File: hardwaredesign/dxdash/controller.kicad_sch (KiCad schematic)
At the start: 67 parts, among them J16 uC_NRST, J17 3V3_uC, J18 SWO, J3 CAN, J4 DEBUG, J5 UART, U2 SN65HVD234, U3 STM32F103RETx, Y1 8MHz

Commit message: controller board added features
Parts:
- removed J3: CAN, Connector_PinHeader_2.54mm:PinHeader_1x03_P2.54mm_Vertical, symbol Connector:Conn_01x03_Pin
- removed R3: 1k, Resistor_SMD:R_1206_3216Metric_Pad1.30x1.75mm_HandSolder, symbol Device:R_Small
- removed R3 (x4): 220, Resistor_SMD:R_1206_3216Metric_Pad1.30x1.75mm_HandSolder, symbol Device:R_Small
- removed TP5V1 (x5): ~, TestPoint:TestPoint_THTPad_D1.0mm_Drill0.5mm, symbol Connector:TestPoint
- removed U2: SN65HVD234, Package_SO:SOIC-8_3.9x4.9mm_P1.27mm, symbol Interface_CAN_LIN:SN65HVD234
- added H1, H2, H3, H4, H5, H6, H7, H8: MountingHole, MountingHole:MountingHole_3.5mm, symbol Mechanical:MountingHole
- added J1: Conn_01x08_Pin, Connector_PinHeader_2.54mm:PinHeader_1x08_P2.54mm_Vertical, symbol Connector:Conn_01x08_Pin
- added TP2, TP3: ~, TestPoint:TestPoint_THTPad_D1.0mm_Drill0.5mm, symbol Connector:TestPoint
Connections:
- net 3V3_uC: now also J1.2 (Pin_2)
- net GND: now also J1.1 (Pin_1)
- net SPI1_CLK: now also J1.3 (Pin_3)
- net SPI1_MOSI: now also J1.4 (Pin_4)
- net uC_pwr_button: now reaches U3.43 (PA10)
- net KEEP_ON: now reaches U3.34 (PB13)
- net DISPLAY_DC: now reaches U3.26 (PB0)
- net DISPLAY_DC: now also J1.6 (Pin_6)
- net DISPLAY_RES: now reaches U3.27 (PB1)
- net DISPLAY_RES: now also J1.5 (Pin_5)
- net BUSWAKE: now reaches U3.33 (PB12)
- net ADC123_IN10 renamed uC_pot1
- net ADC123_IN11 renamed uC_pot2
- net ADC123_IN12: no longer names the net of U3.10 (PC2)
- net ADC123_IN12: now also TP2.1
- net ADC_U_HVDC: no longer names the net of U3.11 (PC3)
- net ADC_U_HVDC: now also TP3.1
- new net 5V: J1.7 (Pin_7)
- no-connect marks 0 -> 1
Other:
- note added: "display connector for ILI9341 and mounting holes"
- note removed: "CAN Transceiver"
- note removed: "CAN termination resistor. 1k does not hurt if the bus is elsewhere terminated, and helps for setup on desk without additional termination."
- note removed: "EN=High enables the transceiver. Low or open would disable it."
- note removed: "Protection resistors for the case, that the controller and the SPI slave are powered from different sources which do not synchronously turn on and off"
- note removed: "todo: EN level selectable via solder jumper"
- note removed: "todo: termination via solder jumper"

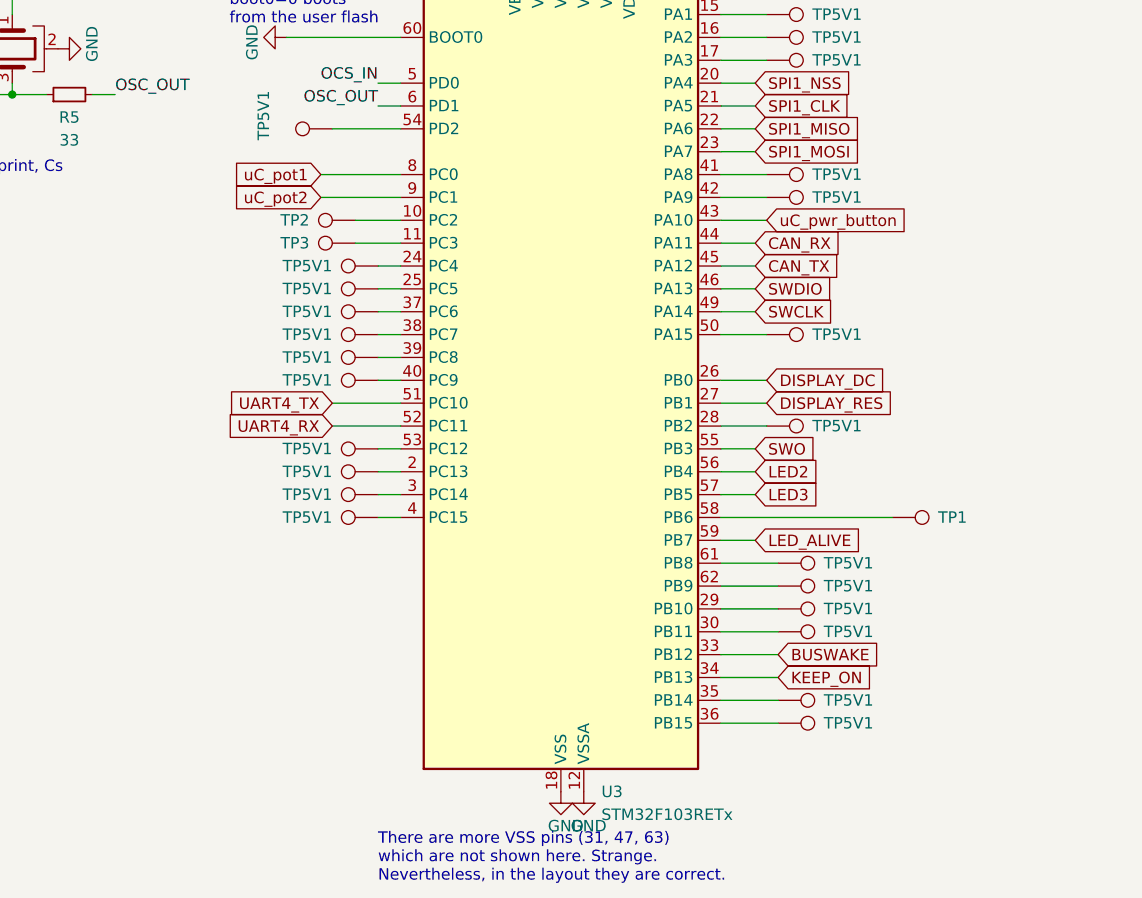
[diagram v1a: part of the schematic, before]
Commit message: added joystick
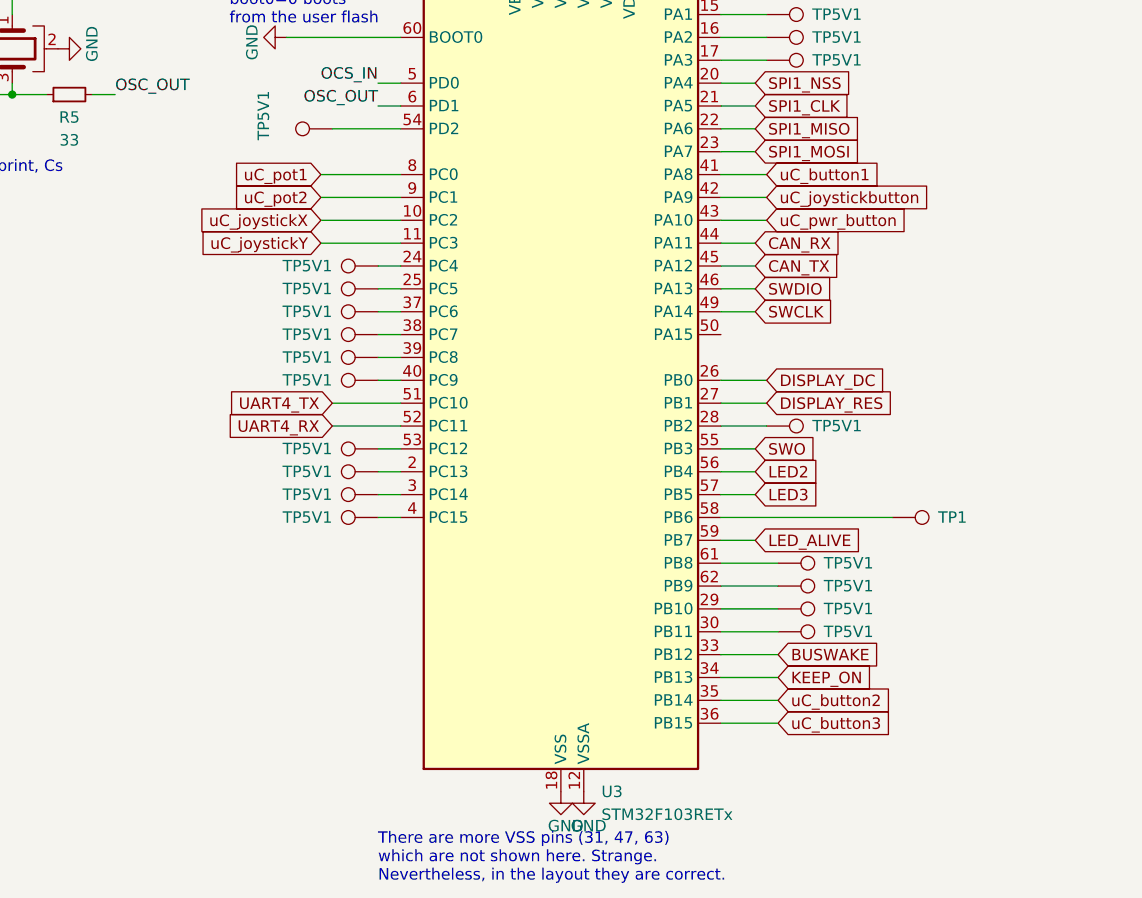
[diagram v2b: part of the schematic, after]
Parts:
- removed TP2, TP3, TP5V1 (x5): ~, TestPoint:TestPoint_THTPad_D1.0mm_Drill0.5mm, symbol Connector:TestPoint
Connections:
- net uC_button3: now reaches U3.36 (PB15)
- net uC_button1: now reaches U3.41 (PA8)
- net uC_joystickX: now reaches U3.10 (PC2)
- net uC_joystickY: now reaches U3.11 (PC3)
- net uC_joystickbutton: now reaches U3.42 (PA9)
- net uC_button2: now reaches U3.35 (PB14)

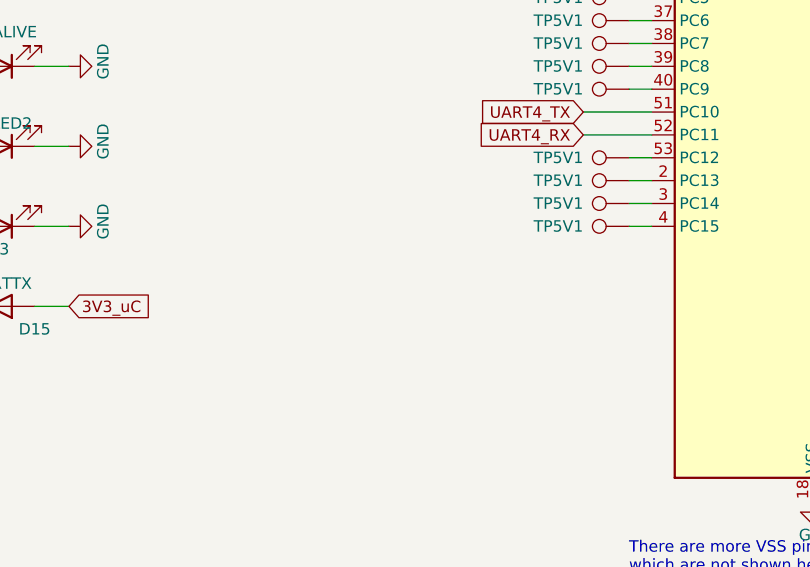
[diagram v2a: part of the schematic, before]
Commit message: added polyfuses
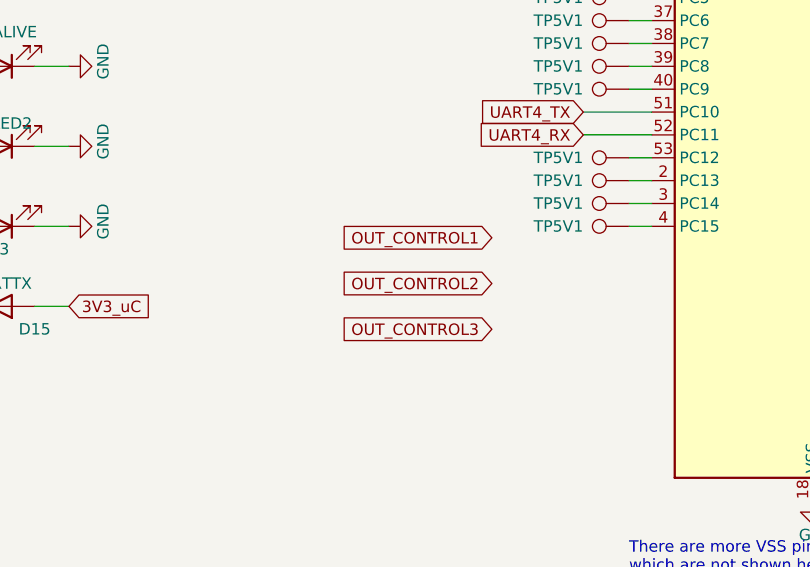
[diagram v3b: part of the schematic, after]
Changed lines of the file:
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@@
+		)
+	)
+	(global_label "OUT_CONTROL3"
+		(shape input)
+		(at 118.11 134.62 180)
+		(fields_autoplaced yes)
+		(effects
+			(font
+				(size 1.27 1.27)
+			)
+			(justify right)
+		)
+		(property "Intersheetrefs" "${INTERSHEET_REFS}"
+			(at 100.7919 134.62 0)
+			(effects
+				(font
+					(size 1.27 1.27)
+				)
+				(justify right)
+				(hide yes)
+			)
 		)
 	)
@@
 		)
 	)
+	(global_label "OUT_CONTROL1"
+		(shape input)
+		(at 118.11 124.46 180)
+		(fields_autoplaced yes)
+		(effects
+			(font
+				(size 1.27 1.27)
+			)
+			(justify right)
+		)
+		(property "Intersheetrefs" "${INTERSHEET_REFS}"
+			(at 100.7919 124.46 0)
+			(effects
+				(font
+					(size 1.27 1.27)
+				)
+				(justify right)
+				(hide yes)
+			)
+		)
+	)
 	(global_label "uC_pot2"
 		(shape input)
@@
 			(effects
 				(font
+					(size 1.27 1.27)
+				)
+				(justify right)
+				(hide yes)
+			)
+		)
+	)
+	(global_label "OUT_CONTROL2"
+		(shape input)
+		(at 118.11 129.54 180)
+		(fields_autoplaced yes)
+		(effects
+			(font
+				(size 1.27 1.27)
+			)
+			(justify right)
+		)
+		(property "Intersheetrefs" "${INTERSHEET_REFS}"
+			(at 100.7919 129.54 0)
+			(effects
+				(font

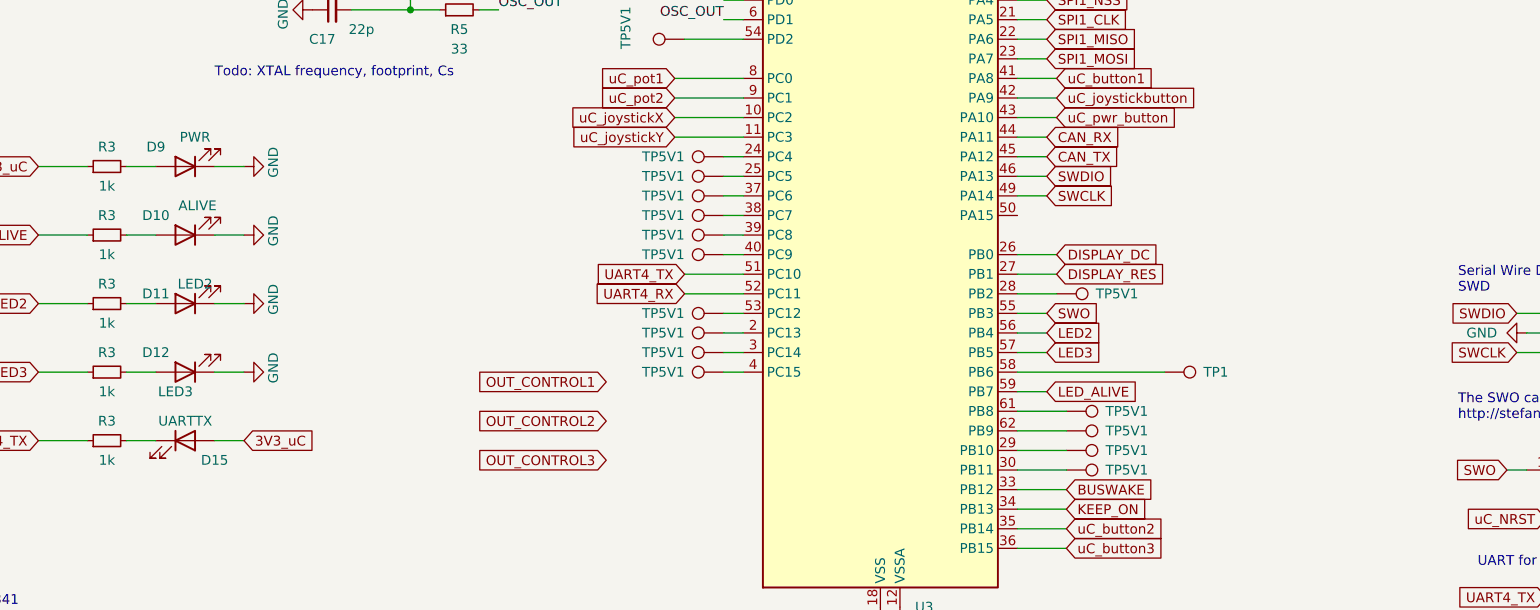
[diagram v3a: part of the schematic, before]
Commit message: added switch inputs. Layout preparation.
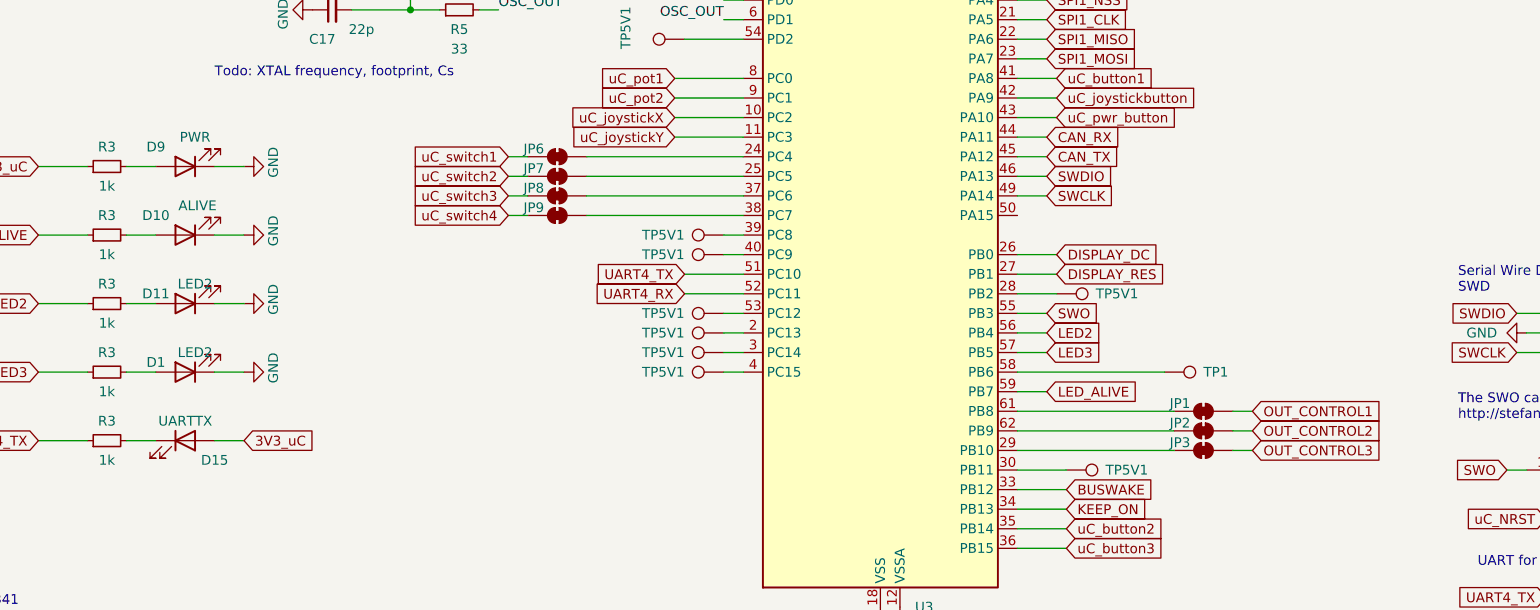
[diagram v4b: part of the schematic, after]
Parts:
- removed D12: LED3, LED_SMD:LED_0805_2012Metric_Pad1.15x1.40mm_HandSolder, symbol Device:LED
- removed TP5V1 (x7): ~, TestPoint:TestPoint_THTPad_D1.0mm_Drill0.5mm, symbol Connector:TestPoint
- added D1: LED2, LED_THT:LED_D5.0mm, symbol Device:LED
- added JP1, JP2, JP3, JP6, JP7, JP8, JP9: SolderJumper_2_Bridged, Jumper:SolderJumper-2_P1.3mm_Bridged_RoundedPad1.0x1.5mm, symbol Jumper:SolderJumper_2_Bridged
- D11: footprint LED_SMD:LED_0805_2012Metric_Pad1.15x1.40mm_HandSolder -> LED_THT:LED_D5.0mm
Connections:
- net GND: now also D1.1 (K)
- net OUT_CONTROL1: now also JP1.2 (B)
- net OUT_CONTROL2: now also JP2.2 (B)
- net OUT_CONTROL3: now also JP3.2 (B)
- net at U3.29 (PB10): now also JP3.1 (A)
- net at U3.38 (PC7): now also JP9.2 (B)
- net at U3.37 (PC6): now also JP8.2 (B)
- net at U3.24 (PC4): now also JP6.2 (B)
- net at U3.25 (PC5): now also JP7.2 (B)
- net at U3.61 (PB8): now also JP1.1 (A)
- net at U3.62 (PB9): now also JP2.1 (A)
- net at R3.2: now also D1.2 (A)
- new net uC_switch1: JP6.1 (A)
- new net uC_switch2: JP7.1 (A)
- new net uC_switch3: JP8.1 (A)
- new net uC_switch4: JP9.1 (A)

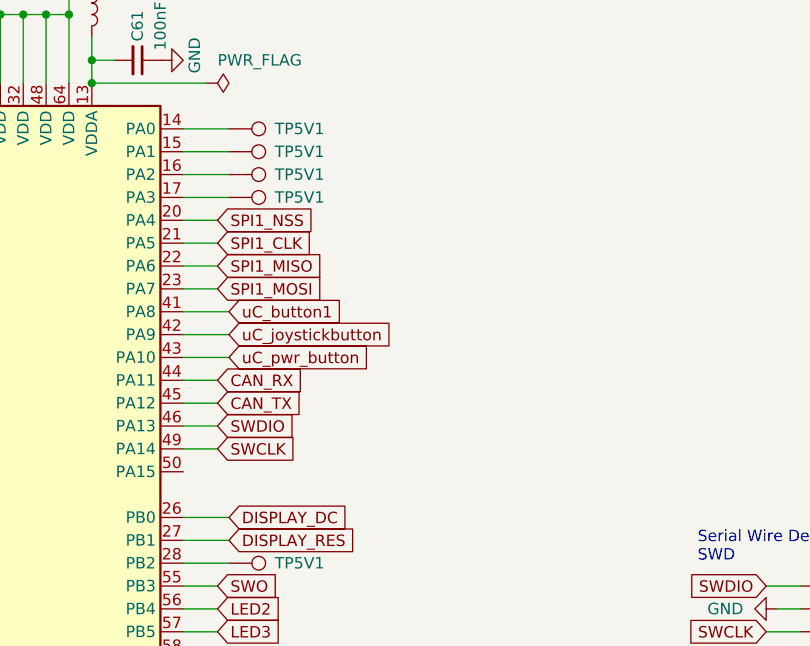
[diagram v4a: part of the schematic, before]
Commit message: board: layout finished
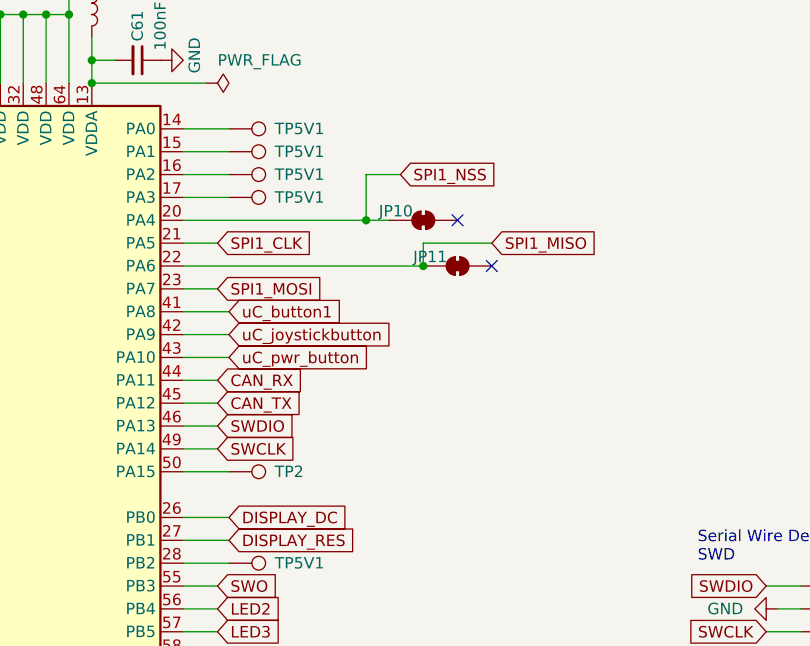
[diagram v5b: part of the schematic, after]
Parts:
- added JP10, JP11: SolderJumper_2_Bridged, Jumper:SolderJumper-2_P1.3mm_Bridged_RoundedPad1.0x1.5mm, symbol Jumper:SolderJumper_2_Bridged
- added TP2: ~, TestPoint:TestPoint_THTPad_D1.0mm_Drill0.5mm, symbol Connector:TestPoint
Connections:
- net SPI1_MISO: now also JP11.1 (A)
- net SPI1_NSS: now also JP10.1 (A)
- net at U3.50 (PA15): now also TP2.1
- no-connect marks 1 -> 3
